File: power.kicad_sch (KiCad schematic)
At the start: 29 parts, among them U2 LMR51635XDDCR, U3 AMS1117

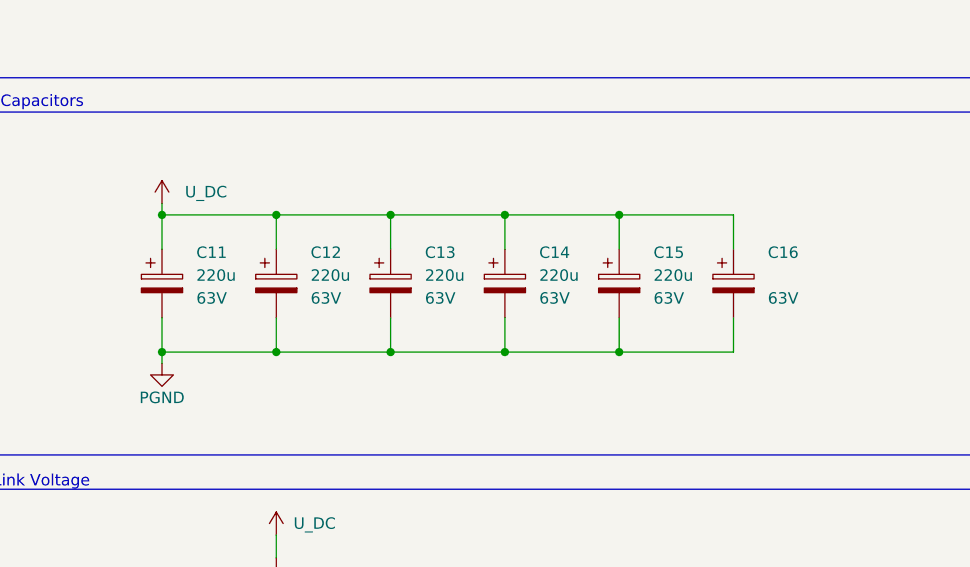
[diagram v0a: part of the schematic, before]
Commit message: Analog current filters were removed, some footprints were fixed and initial rough layout has been made.
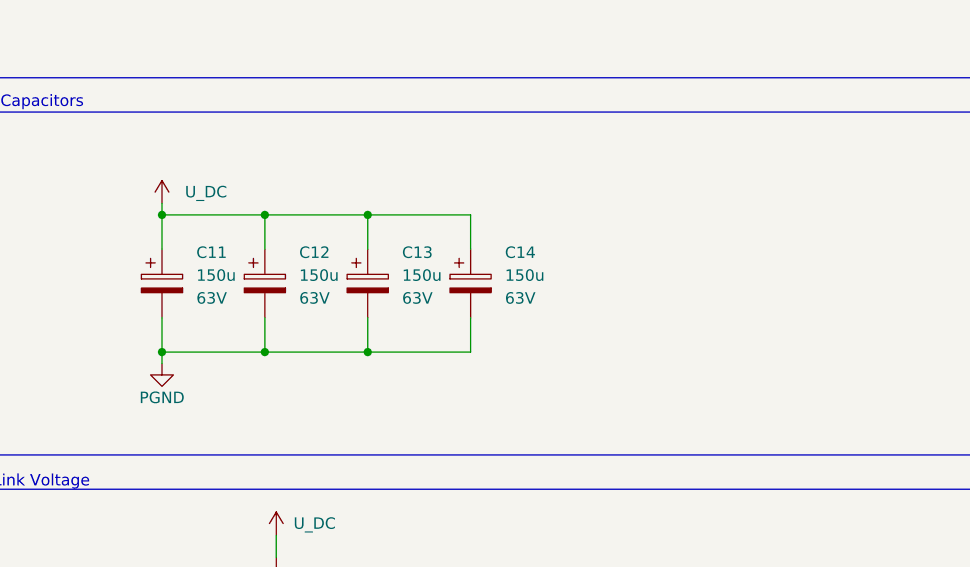
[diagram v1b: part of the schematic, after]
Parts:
- removed C15, C16: 220u, symbol NanoGaN:C_Polarized_FZ1J221M1313
- C11, C12, C13, C14: value 220u -> 150u; footprint (none) -> Capacitor_SMD:CP_Elec_10x10.5; LCSC C5260762 -> C22383765

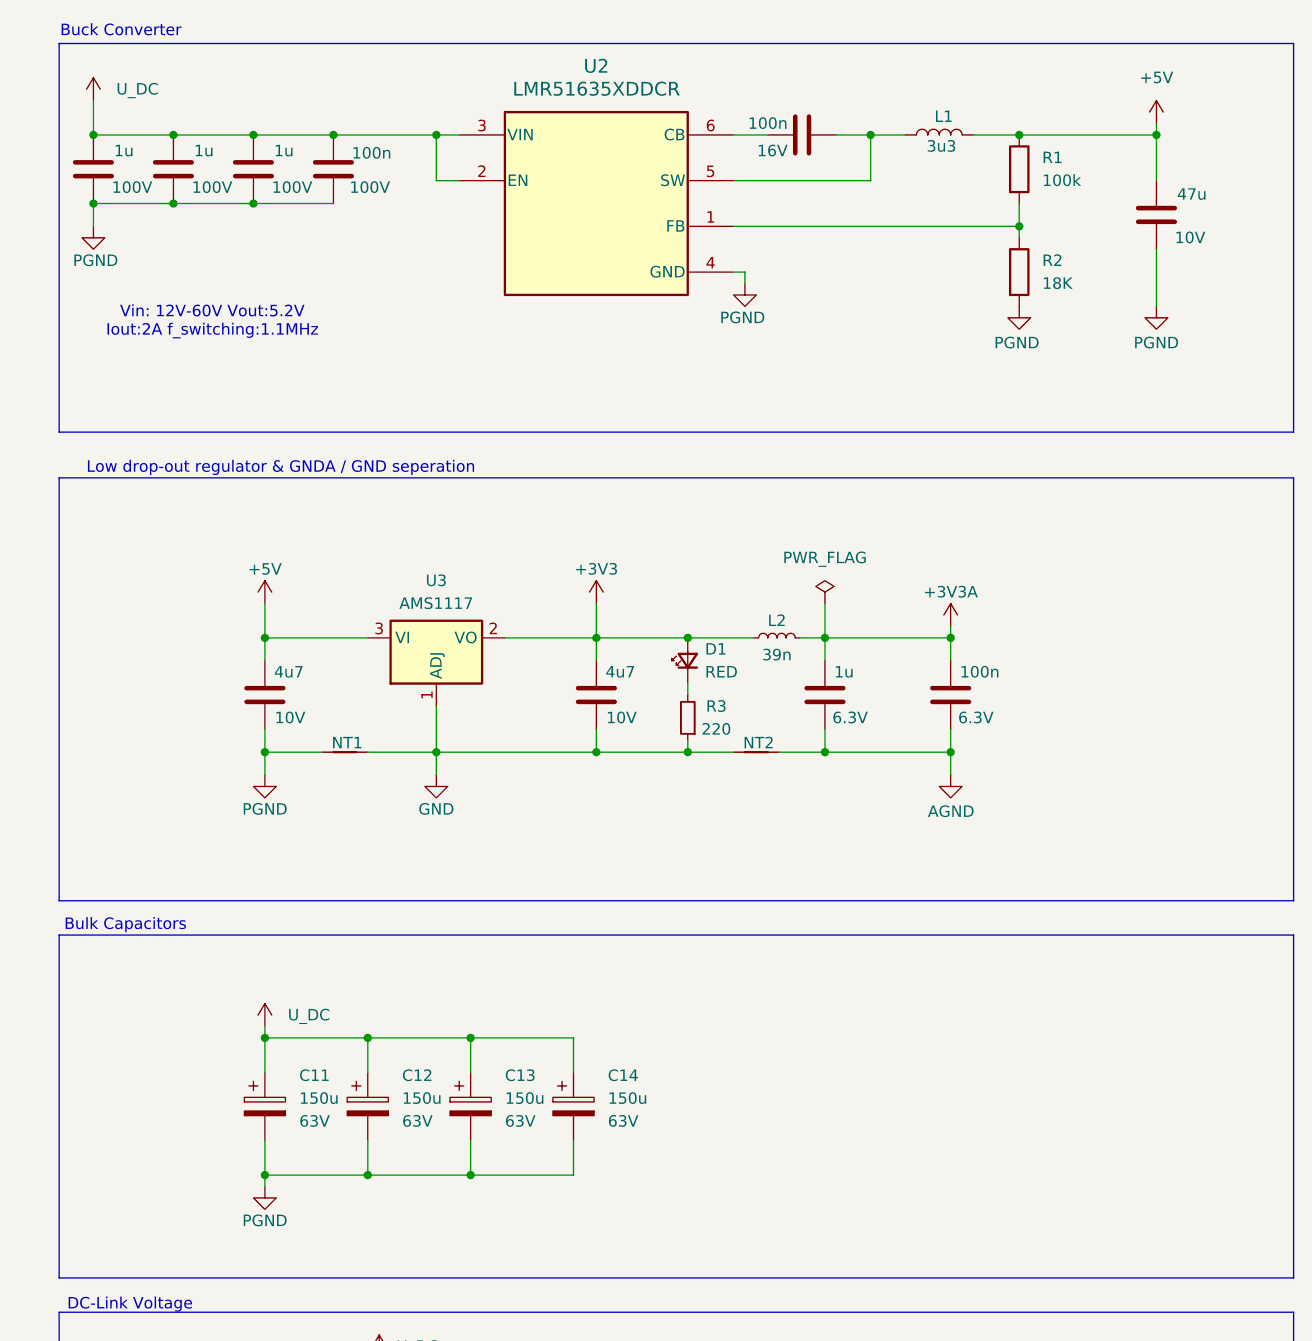
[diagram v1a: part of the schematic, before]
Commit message: Updated the DC/DC converter from I_out = 2A to 3.5A  and fsw = 1.1MHz to 400kHz
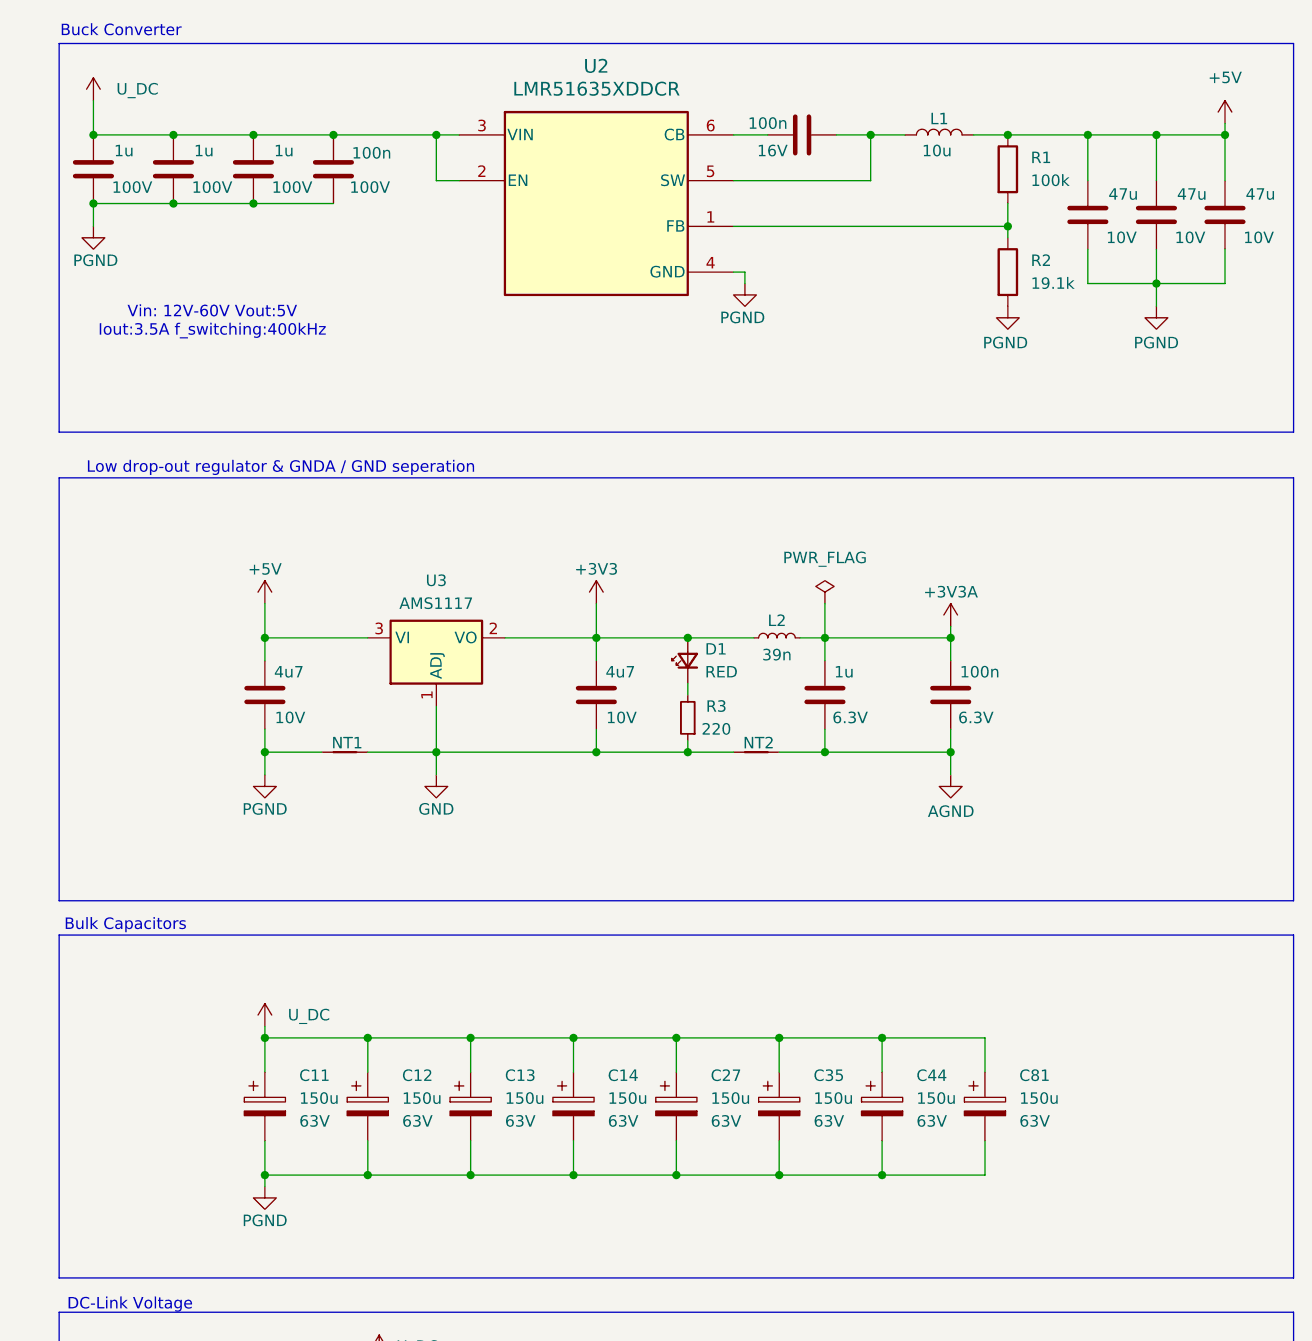
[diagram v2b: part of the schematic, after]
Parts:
- removed L1: 3u3, NanoGaN:XAL40XX, symbol NanoGaN:XAL4030-332MEC
- added C27, C35, C44, C81: 150u, Capacitor_SMD:CP_Elec_10x10.5, symbol NanoGaN:C_Polarized_FZ1J221M1313
- added C82, C86: 47u, Capacitor_SMD:C_1206_3216Metric, symbol Device:C
- added L1: 10u, NanoGaN:IND_XAL60XX-240H_COC, symbol Device:L
- R2: value 18K -> 19.1k; footprint Resistor_SMD:R_0603_1608Metric -> Resistor_SMD:R_0402_1005Metric; LCSC C25810 -> C52036; Manufacturer_Name 0603WAF1802T5E -> 0402WGF1912TCE
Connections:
- net +5V: now also C82.1, C86.1, L1.2
- net PGND: now also C27.2, C35.2, C44.2, C81.2, C82.2, C86.2
- net U_DC: now also C27.1, C35.1, C44.1, C81.1
- net at C5.2, U2.5 (SW): now also L1.1
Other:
- note added: "Vin: 12V-60V Vout:5V Iout:3.5A f_switching:400kHz"
- note removed: "Vin: 12V-60V Vout:5.2V Iout:2A f_switching:1.1MHz"
- moved on the sheet: R1, R2

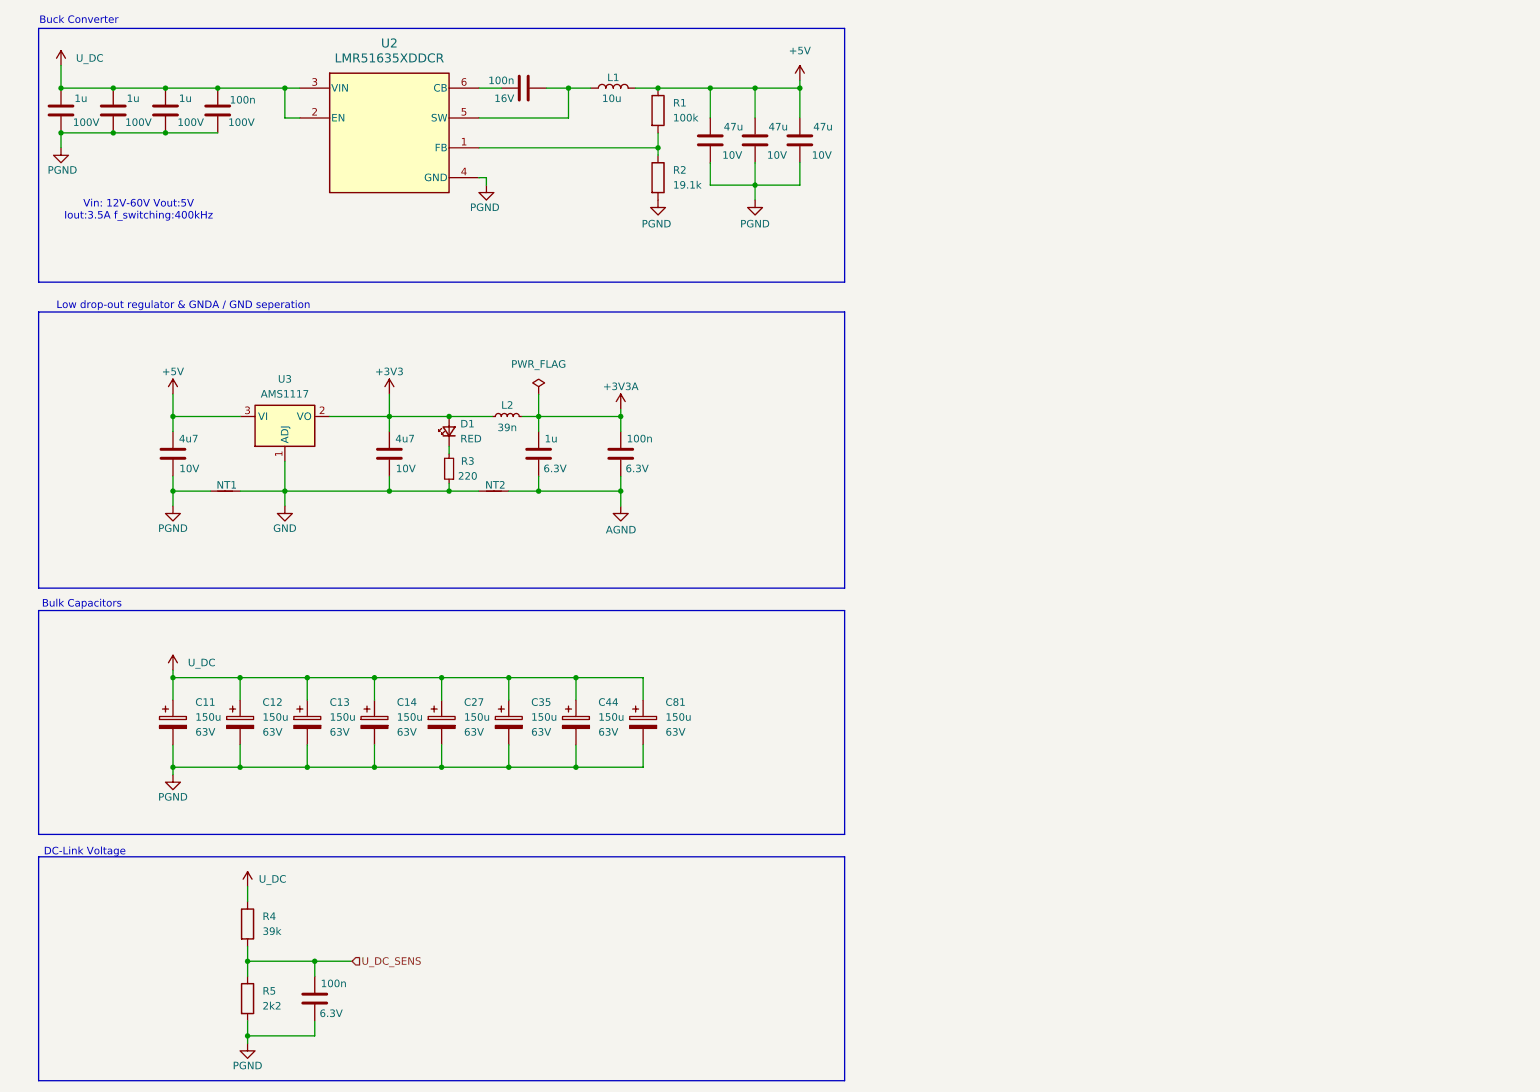
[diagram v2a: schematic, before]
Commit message: pdf export and small fixes
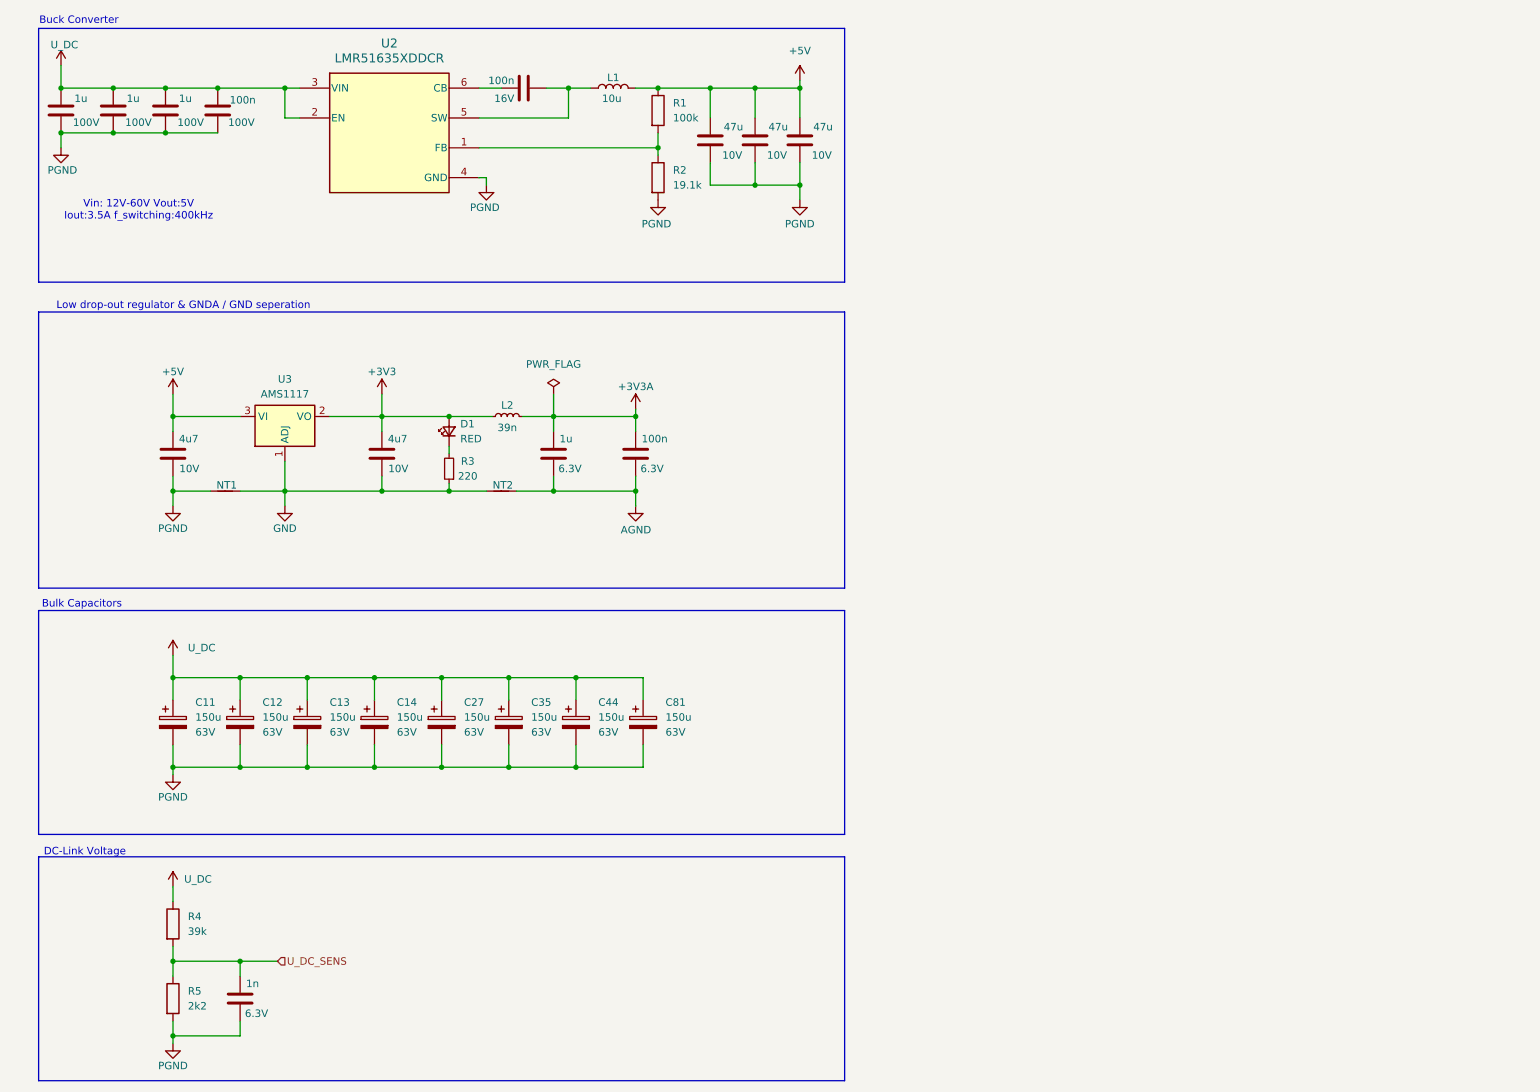
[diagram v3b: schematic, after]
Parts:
- C18: value 100n -> 1n; footprint Capacitor_SMD:C_0402_1005Metric -> Capacitor_SMD:C_0201_0603Metric; LCSC C424821 -> C541214
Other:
- moved on the sheet: NT2, R4, R5
